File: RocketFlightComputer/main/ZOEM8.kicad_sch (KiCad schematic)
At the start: 9 parts, among them U3 U-BLOX_ZOE_M8Q-0-10, Y4 32.768kHz

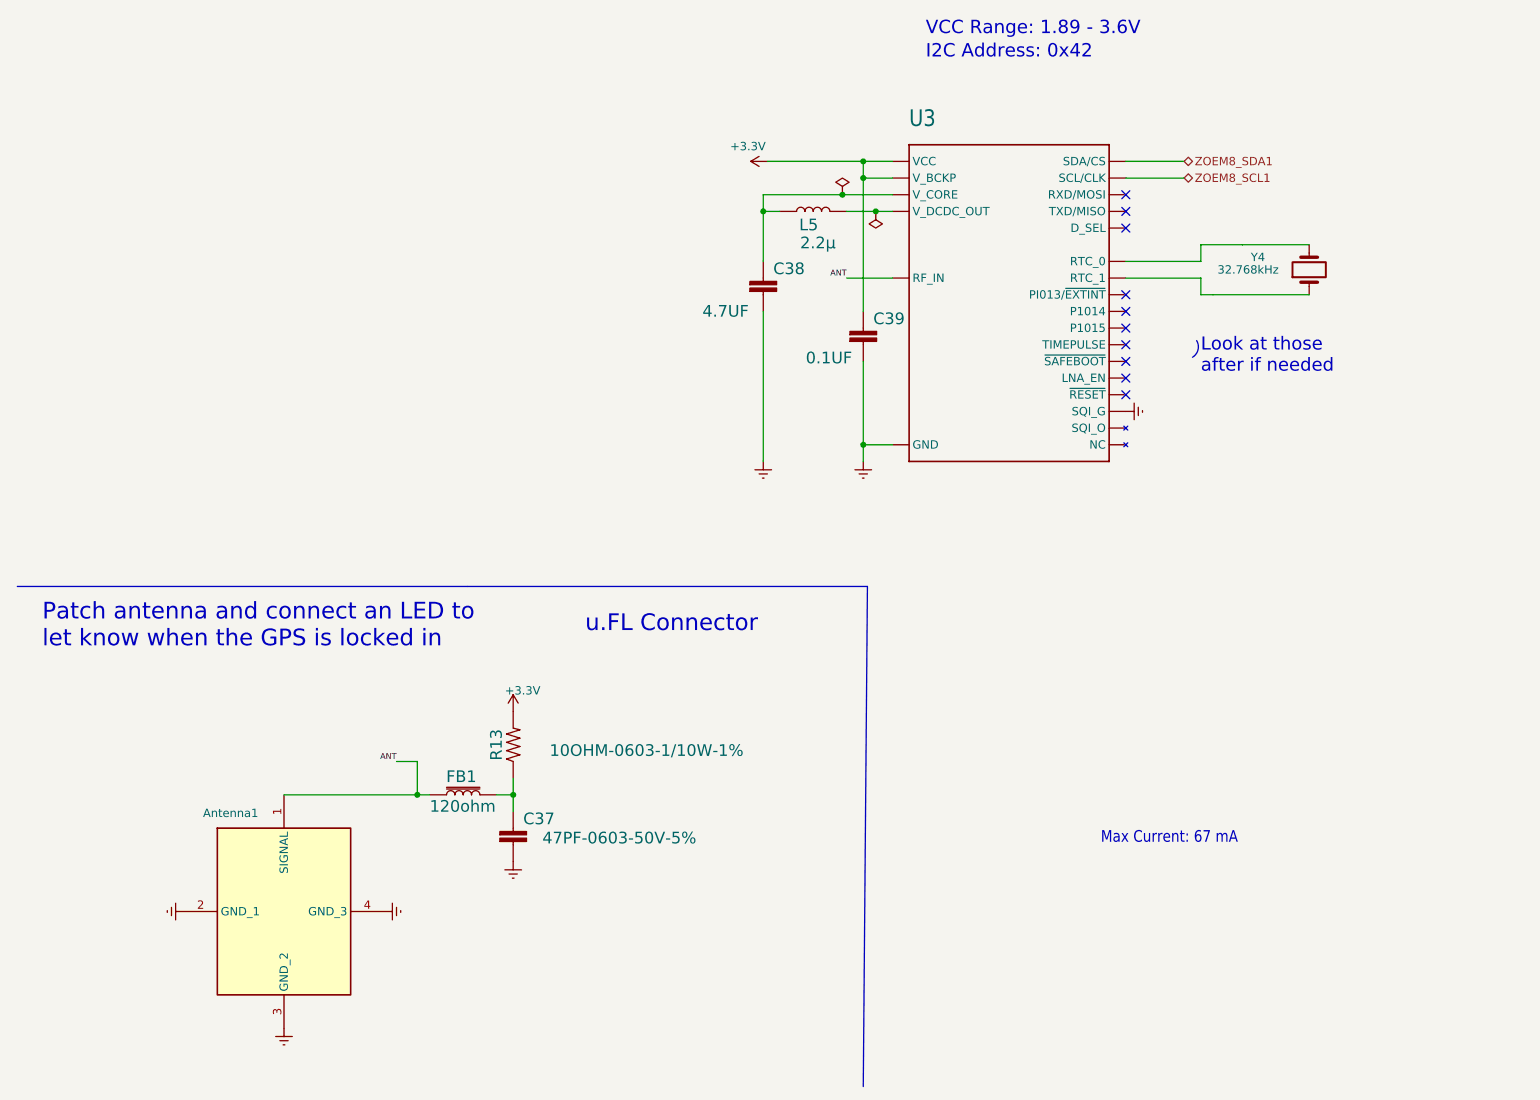
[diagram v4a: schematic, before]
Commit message: Layout of PCB mostly done
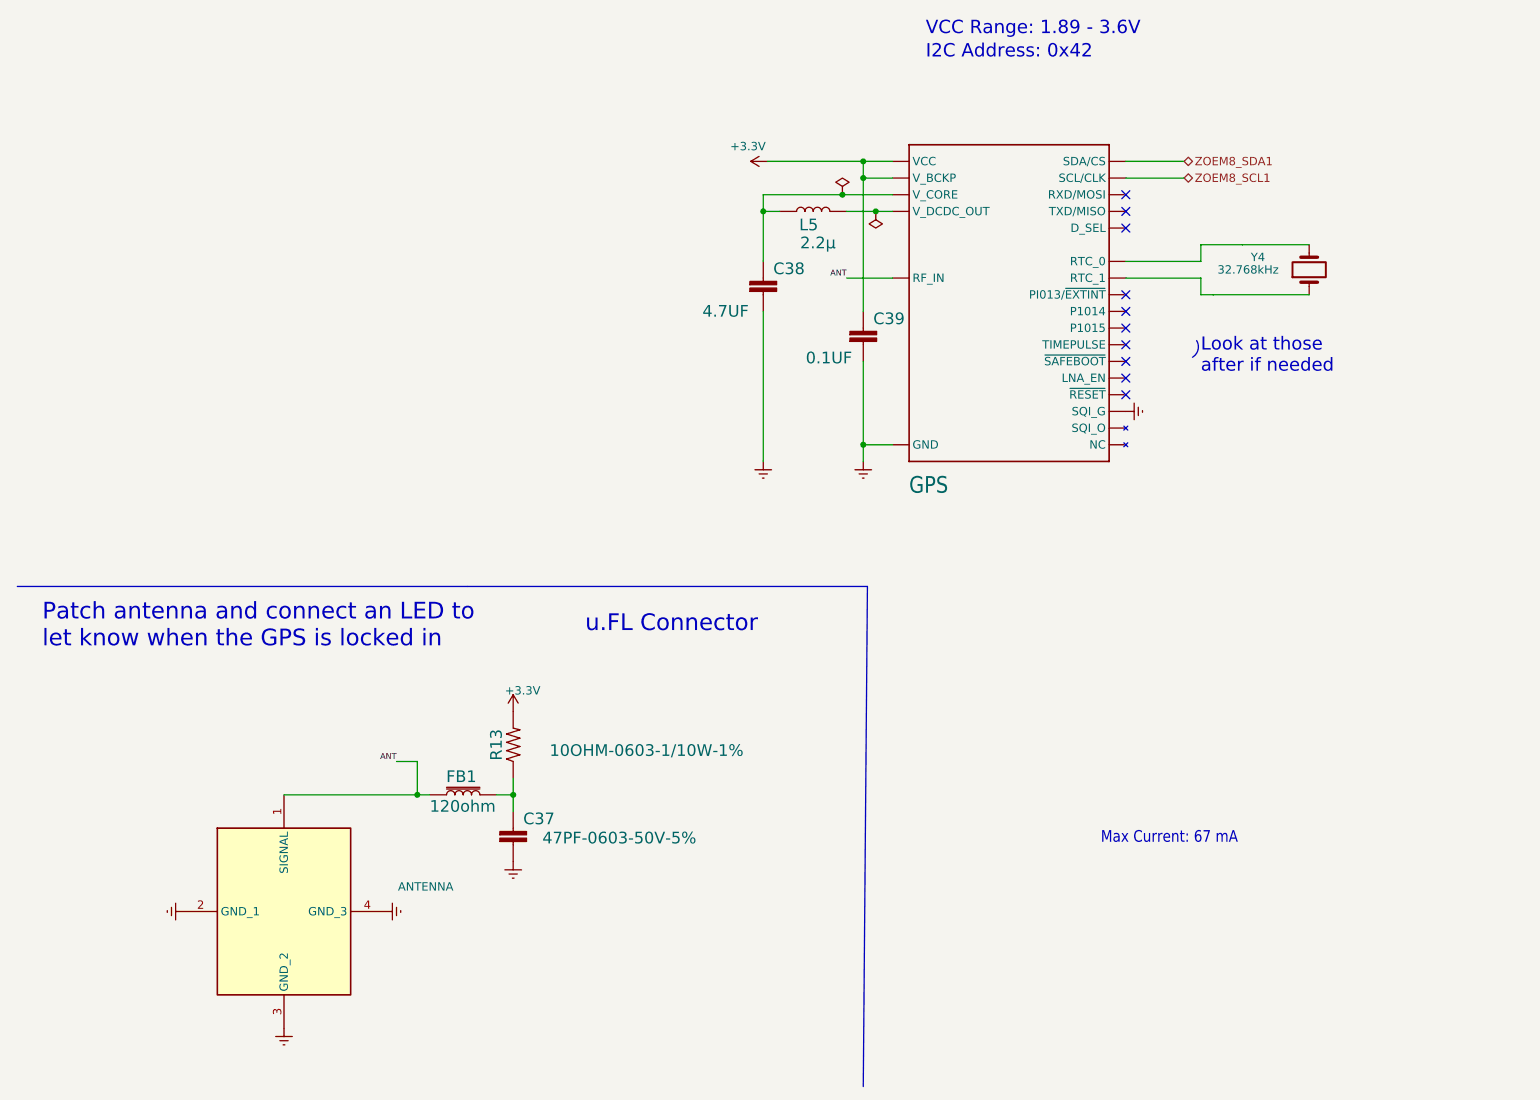
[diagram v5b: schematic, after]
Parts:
- CONMHF1-SMD-G-T1: renamed from Antenna1; value CONMHF1-SMD-G-T -> ANTENNA
- U-BLOX_ZOE_M8Q-0-10: renamed from U3; value U-BLOX_ZOE_M8Q-0-10 -> GPS
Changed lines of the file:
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@@
 		(on_board yes)
 		(dnp no)
-		(property "Reference" "U3"
+		(property "Reference" "U-BLOX_ZOE_M8Q-0-10"
 			(at 148.59 52.07 0)
 			(effects
@@
 				)
 				(justify left bottom)
-			)
-		)
-		(property "Value" "U-BLOX_ZOE_M8Q-0-10"
+				(hide yes)
+			)
+		)
+		(property "Value" "GPS"
 			(at 148.59 107.95 0)
 			(effects
@@
 				)
 				(justify left bottom)
-				(hide yes)
 			)
 		)
@@
 			)
 		)
-		(property "Description" ""
+		(property "Description" "U-BLOX_ZOE_M8Q-0-10"
 			(at 163.83 80.01 0)
 			(effects
@@
 			(project "main"
 				(path "/27195d1d-92b2-40df-ada5-3b20841577e7/29f0379a-3100-4813-a2e2-86f2e88b3e64"
-					(reference "U3")
+					(reference "U-BLOX_ZOE_M8Q-0-10")
 					(unit 1)
 				)
@@
 		(on_board yes)
 		(dnp no)
-		(property "Reference" "Antenna1"
+		(property "Reference" "CONMHF1-SMD-G-T1"
 			(at 45.212 156.464 0)
 			(effects
@@
 					(size 1.27 1.27)
 				)
-			)
-		)
-		(property "Value" "CONMHF1-SMD-G-T"
+				(hide yes)
+			)
+		)
+		(property "Value" "ANTENNA"
 			(at 74.93 167.6714 0)
 			(effects
@@
 					(size 1.27 1.27)
 				)
-				(hide yes)
 			)
 		)
@@
 			)
 		)
-		(property "Description" "Body Features: Body Material Copper Alloy | Body Plating Material Gold | Configuration Features: Number of Positions 1 | Number of Coaxial Contacts 1 | Electrical Characteristics: Impedance 50 OHM | Mechanical Attachment: RF Connector Coupling Mechanism Snap-On | Connector Mounting Type Board Mount | Operation/Application: Circuit Application Signal | Operating Frequency 6 GHZ | Other: Dielectric Material LCP | Product Type Features: Connector & Contact Terminates To Printed Circuit Board | Connector System"
+		(property "Description" "CONMHF1-SMD-G-T"
 			(at 38.1 171.45 0)
 			(effects
@@
 			(project ""
 				(path "/27195d1d-92b2-40df-ada5-3b20841577e7/29f0379a-3100-4813-a2e2-86f2e88b3e64"
-					(reference "Antenna1")
-					(unit 1)
-				)
+					(reference "CONMHF1-SMD-G-T1")
+					(unit 1)
+				)

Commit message: Preliminary layout done but need to rearrange sd card and such to have the best routing
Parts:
- Y4: footprint Crystal:Crystal_SMD_2012-2Pin_2.0x1.2mm -> footprint:830050789
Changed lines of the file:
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@@
 			)
 		)
-		(property "Footprint" "Crystal:Crystal_SMD_2012-2Pin_2.0x1.2mm"
+		(property "Footprint" "footprint:830050789"
 			(at 209.55 73.66 0)
 			(effects

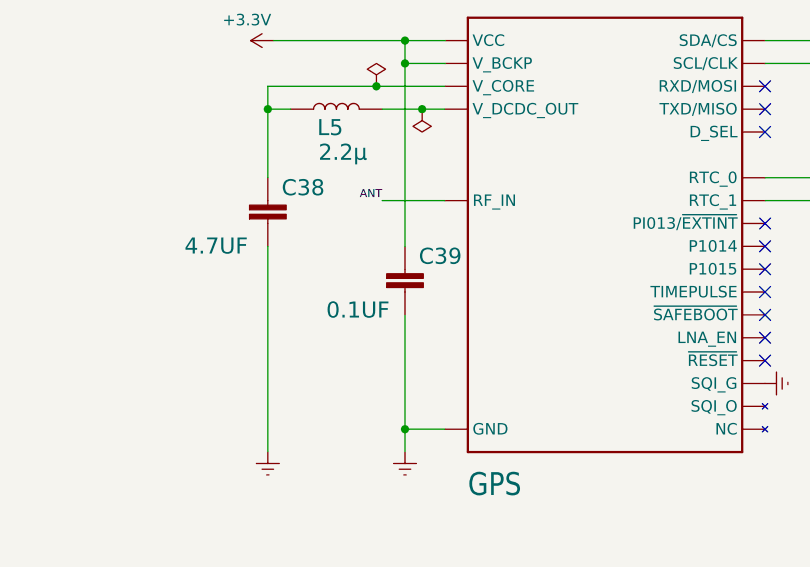
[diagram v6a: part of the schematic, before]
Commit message: Addition of teensy example and milestone on routing completed, missing a few components to connect
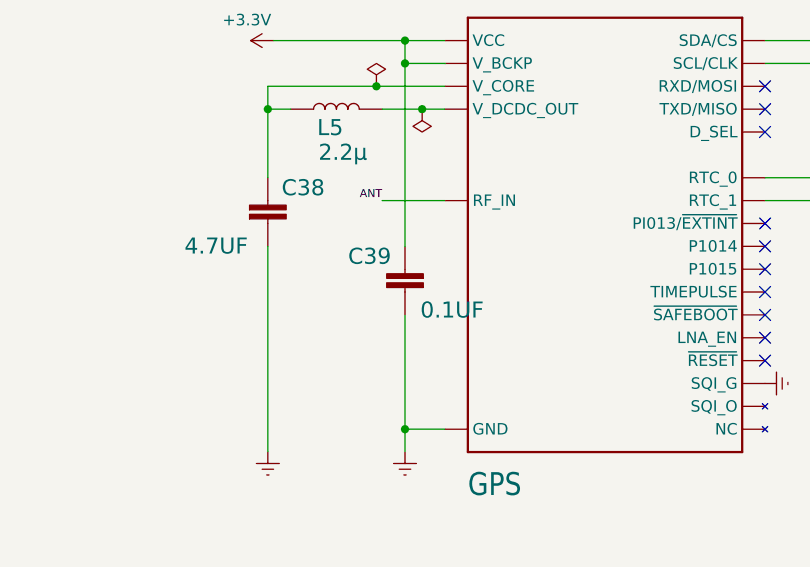
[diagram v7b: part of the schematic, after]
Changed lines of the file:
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@@
 		(lib_id "SparkFun_ZOE-M8Q GPS-eagle-import:0.1UF-0603-25V-(+80/-20%)")
 		(at 141.605 85.09 0)
+		(mirror y)
 		(unit 1)
 		(exclude_from_sim no)
@@
 		(dnp no)
 		(property "Reference" "C39"
-			(at 143.129 82.169 0)
+			(at 140.081 82.169 0)
 			(effects
 				(font
@@
 		)
 		(property "Value" "0.1UF"
-			(at 132.842 88.138 0)
+			(at 150.368 88.138 0)
 			(effects
 				(font

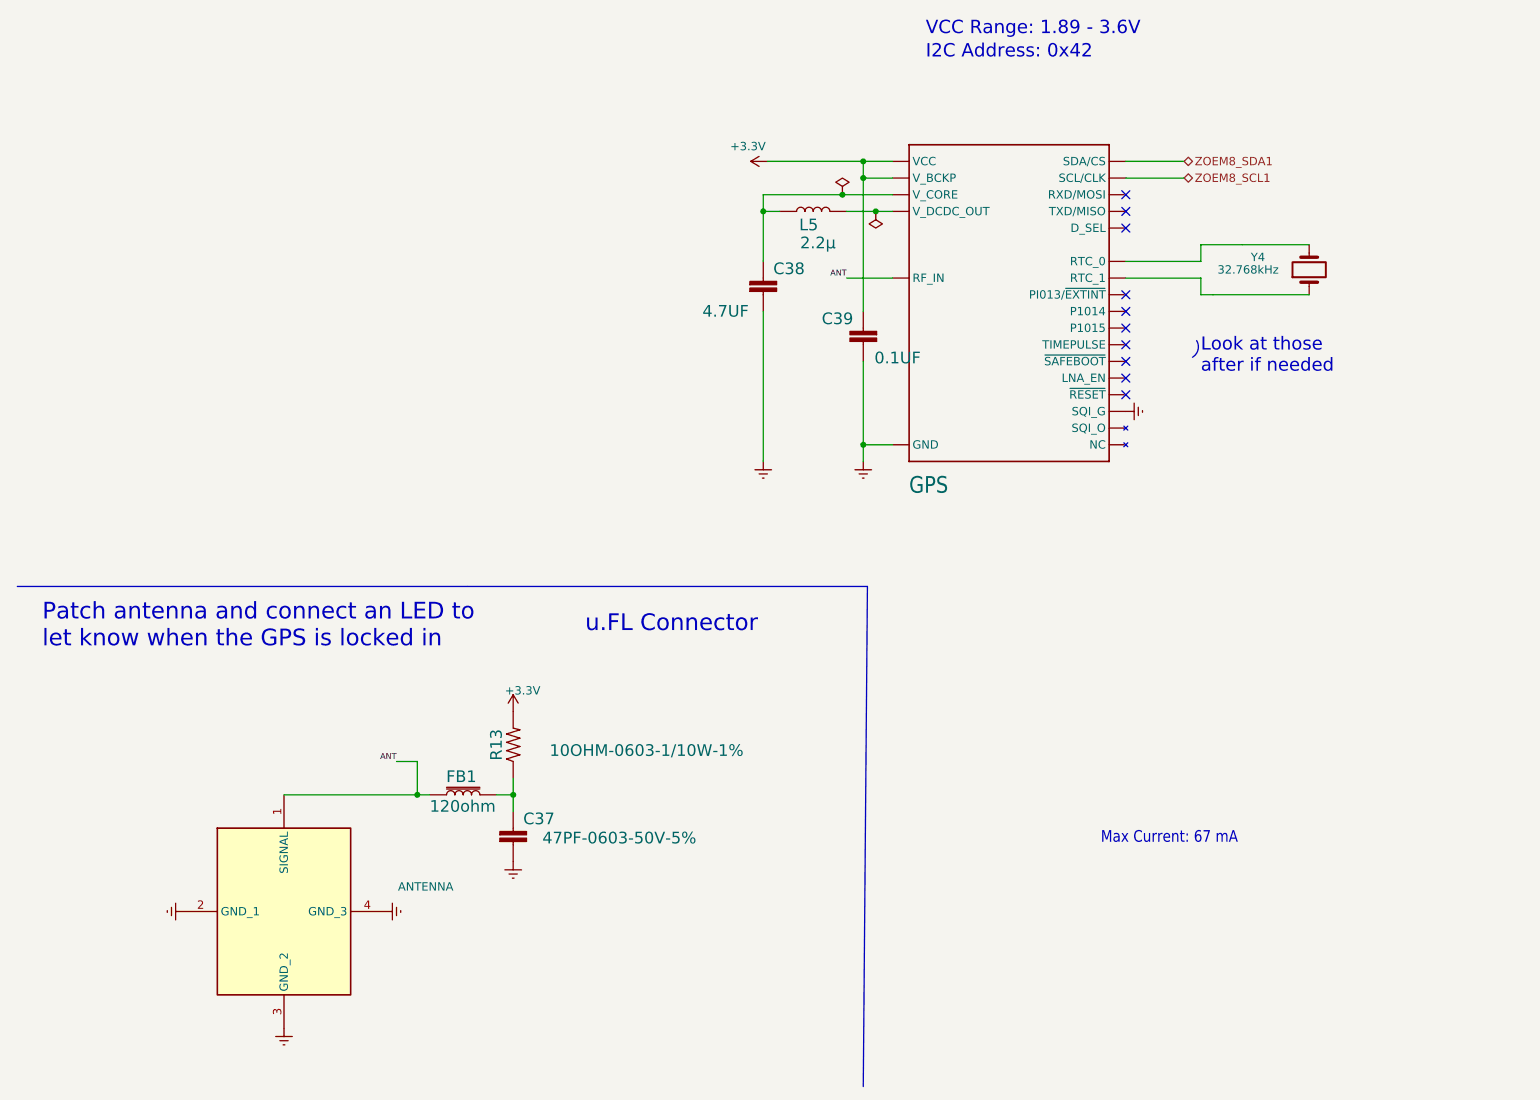
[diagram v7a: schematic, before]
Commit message: First pass of verification and validation of pcb design
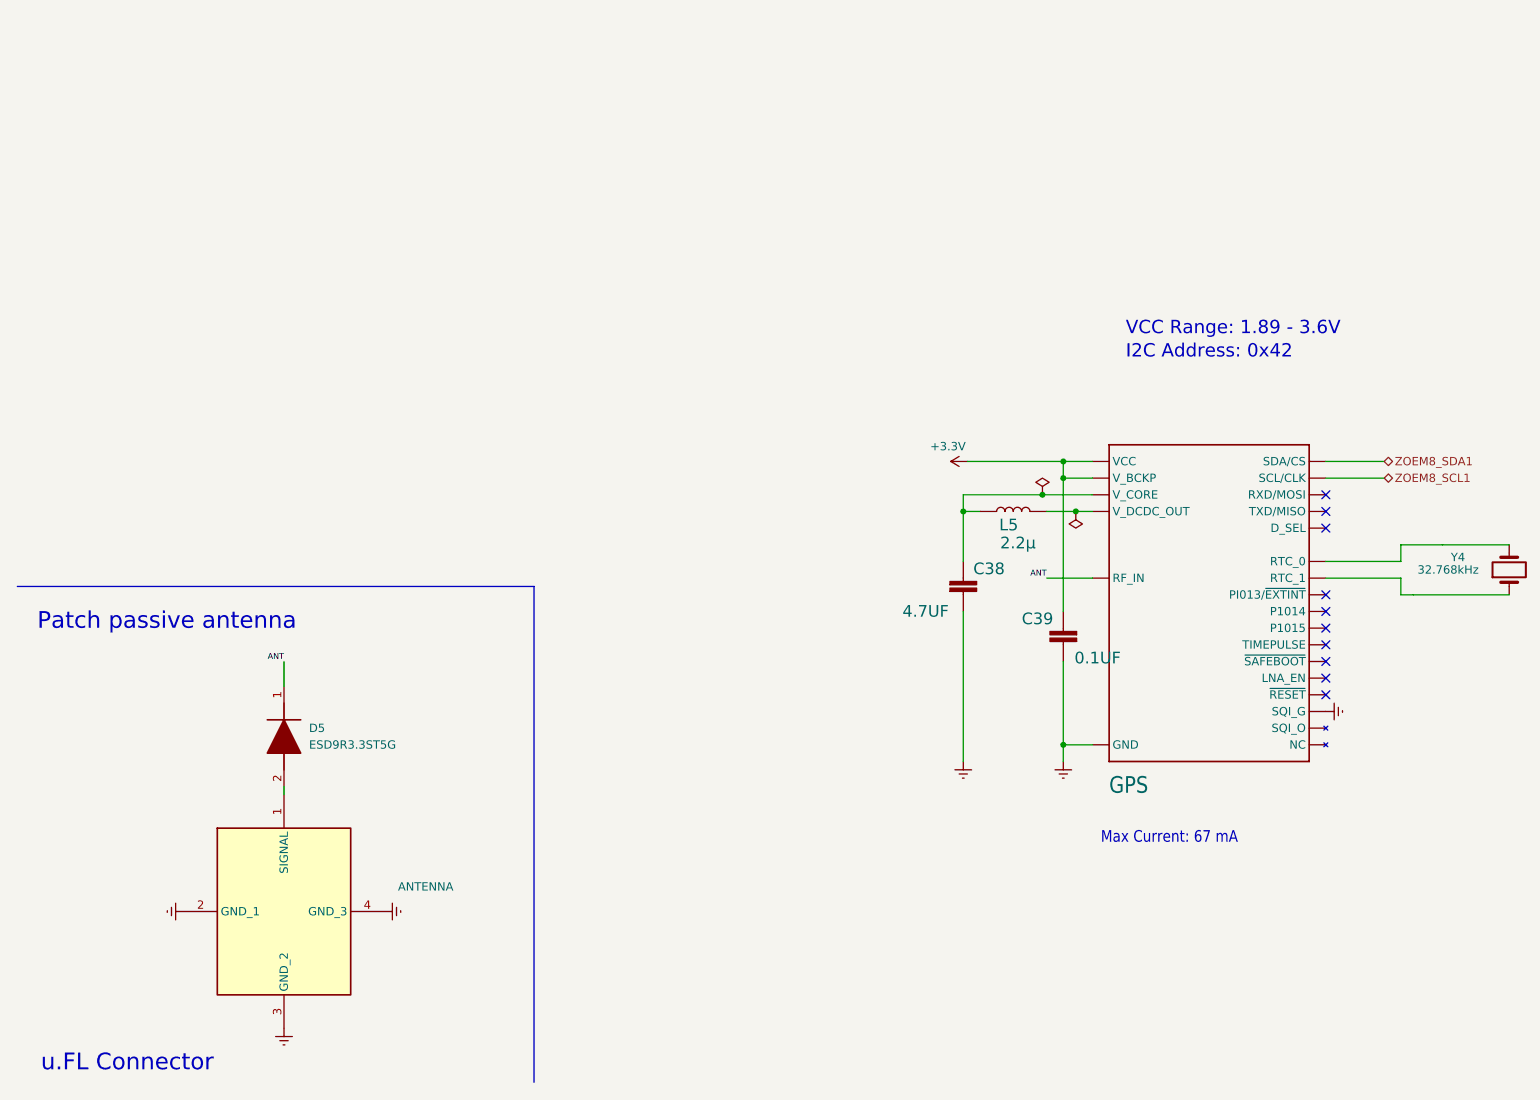
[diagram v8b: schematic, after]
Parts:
- removed C37: 47PF-0603-50V-5%, Resistor_SMD:R_0603_1608Metric_Pad0.98x0.95mm_HandSolder, symbol SparkFun_ZOE-M8Q GPS-eagle-import:47PF-0603-50V-5%
- removed FB1: 120ohm, Resistor_SMD:R_0603_1608Metric_Pad0.98x0.95mm_HandSolder, symbol SparkFun_ZOE-M8Q GPS-eagle-import:FERRITE_BEAD-120_OHM-0402
- removed R13: 10OHM-0603-1/10W-1%, Resistor_SMD:R_0603_1608Metric_Pad0.98x0.95mm_HandSolder, symbol SparkFun_ZOE-M8Q GPS-eagle-import:10OHM-0603-1/10W-1%
- added D5: ESD9R3.3ST5G, footprint:ESD9R3_3ST5G, symbol ESD9R3_3ST5G:ESD9R3.3ST5G
- L5: footprint Resistor_SMD:R_0603_1608Metric_Pad0.98x0.95mm_HandSolder -> ZOE-M8Q:0806
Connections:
- net ANT: now also D5.1 (K); no longer CONMHF1-SMD-G-T1.1 (SIGNAL)
- new net: CONMHF1-SMD-G-T1.1 (SIGNAL), D5.2 (A)
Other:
- note added: "Patch passive antenna"
- note removed: "Look at those after if needed"
- note removed: "Patch antenna and connect an LED to let know when the GPS is locked in"
- moved on the sheet: C38, C39, L5, Y4
